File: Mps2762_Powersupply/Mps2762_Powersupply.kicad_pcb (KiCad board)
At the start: 4 copper layers, 56.7 x 37.7 mm, 52 parts, among them J1 124018312112A, J2 Conn_01x08_Pin, J3 Conn_01x02_Pin, J4 Conn_01x02_Pin, SW1 SW_DIP_x03, U1 MP2762AGV-0000-P, U2 CH224K, U3 AP62600SJ-7

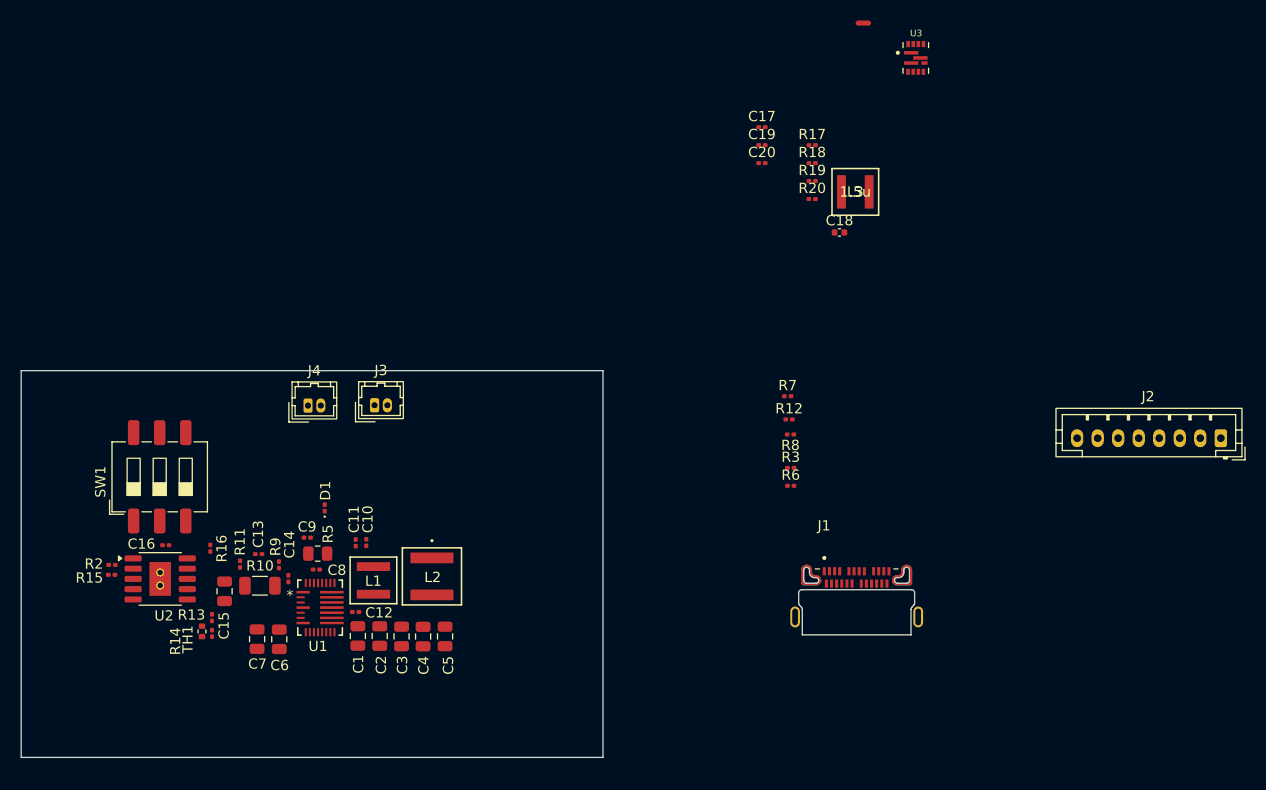
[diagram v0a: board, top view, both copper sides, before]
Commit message: layout updated
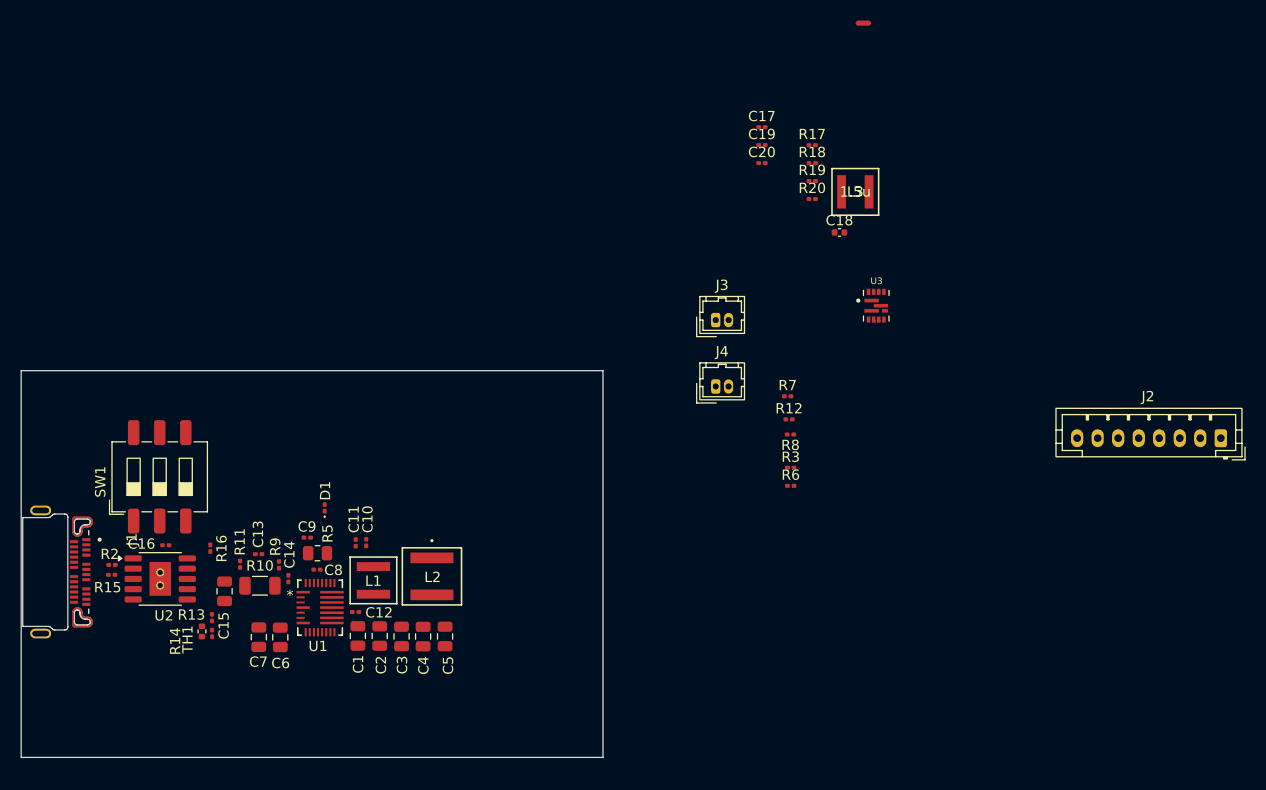
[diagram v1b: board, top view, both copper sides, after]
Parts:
- moved J1 79.6 mm to (108.7, 107.0), turned to -90 degrees
- moved J4 39.8 mm to (174.5, 88.9)
- moved J3 34.3 mm to (174.5, 82.5)
- moved U3 24.5 mm to (190.1, 81.0)
- moved C7 0.25 mm to (129.9, 113.3)
- moved C6 0.21 mm to (132.0, 113.4)
- moved C8 0.06 mm to (135.6, 106.8)

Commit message: added gnd vias
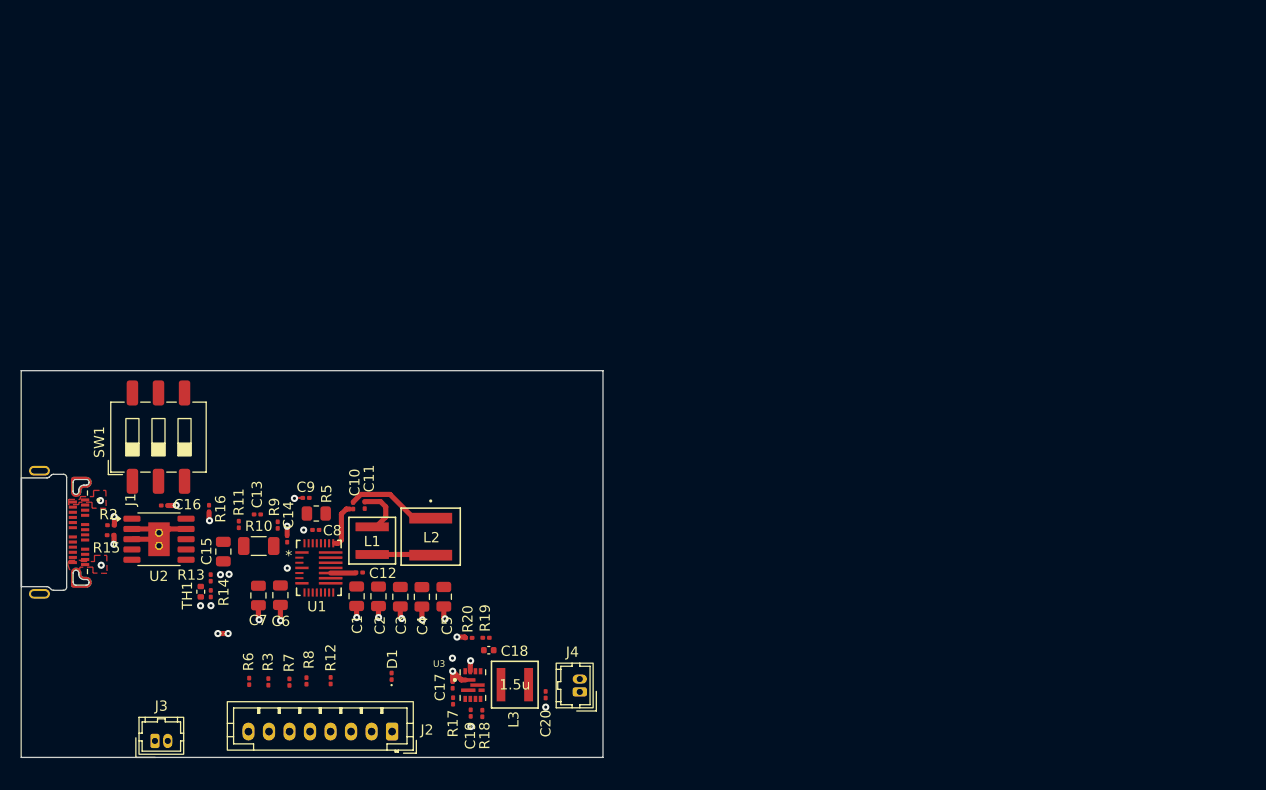
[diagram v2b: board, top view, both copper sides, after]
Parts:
- moved NT0 86.2 mm to (126.4, 113.0), turned to 180 degrees
- moved J2 85.7 mm to (142.9, 122.5)
- moved J3 68.3 mm to (119.8, 123.5)
- moved R17 64.5 mm to (148.9, 119.6), turned to -90 degrees
- moved R18 62.5 mm to (151.7, 120.8), turned to 90 degrees
- moved C19 62.2 mm to (150.6, 120.8), turned to -90 degrees
- moved C17 62.2 mm to (148.8, 118.0), turned to -90 degrees
- moved L3 58.4 mm to (154.9, 118.0)
- moved R6 56.1 mm to (129.0, 117.7), turned to 90 degrees
- moved R7 56.0 mm to (132.9, 117.7), turned to -90 degrees
- moved C20 55.9 mm to (157.9, 119.0), turned to 90 degrees
- moved R3 55.0 mm to (130.9, 117.7), turned to 90 degrees
- moved R19 54.7 mm to (152.1, 113.4)
- moved R20 54.3 mm to (150.4, 113.4)
- moved U3 54.0 mm to (150.8, 118.0)
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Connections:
- J2 pad 1: /PROCHOT -> /ACOK
- J2 pad 2: /INT -> /IAM
- J2 pad 3: /MCU_ACOK -> /IBM
- J2 pad 5: /IBM -> /SCL
- J2 pad 6: /IAM -> /SDA
- J2 pad 7: /SDA -> /INT
- J2 pad 8: /SCL -> /PROCHOT
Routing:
- net PGND: track 0.00 -> 27.4 mm, vias 0 -> 25
- net /SW1: track 0.00 -> 8.82 mm
- net /SW3: track 0.00 -> 8.22 mm
- net /SW2: track 0.00 -> 4.97 mm
- net /BST1: track 0.00 -> 4.46 mm
- net AGND: track 0.00 -> 0.03 mm, vias 0 -> 4
- added copper zone on In1.Cu, net AGND
- added copper zone on F.Cu, net PGND
- added copper zone on In2.Cu, net PGND

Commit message: almost routed
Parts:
- removed NT0: NetTie_2, NetTie:NetTie-2_SMD_Pad0.5mm
- C10: moved to B.Cu
- moved J3 46.3 mm to (161.6, 103.6), turned to 90 degrees
- moved R6 38.6 mm to (159.7, 94.2), turned to -90 degrees
- moved R3 36.2 mm to (158.4, 94.2), turned to -90 degrees
- moved J2 36.1 mm to (160.0, 90.7)
- moved R12 28.6 mm to (153.9, 94.5)
- moved R7 27.6 mm to (147.5, 94.3), turned to 90 degrees
- moved R8 26.0 mm to (145.9, 94.3), turned to 90 degrees
- moved D1 18.8 mm to (130.4, 103.2)
- moved L2 16.2 mm to (136.5, 90.9), turned to 0 degrees
- moved TH1 13.9 mm to (137.2, 114.1)
- moved C7 13.8 mm to (143.5, 106.7)
- moved R2 13.0 mm to (122.5, 91.5), turned to -90 degrees
- moved R15 12.8 mm to (119.9, 91.5), turned to -90 degrees
- moved R16 12.3 mm to (117.1, 91.5), turned to -90 degrees
- moved R14 12.1 mm to (136.0, 114.6)
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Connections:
- J2 pad 1: /ACOK -> /PROCHOT
- J2 pad 2: /IAM -> /INT
- J2 pad 3: /IBM -> /MCU_ACOK
- J2 pad 5: /SCL -> /IBM
- J2 pad 6: /SDA -> /IAM
- J2 pad 7: /INT -> /SDA
- J2 pad 8: /PROCHOT -> /SCL
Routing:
- net +3.3V: track 0.00 -> 47.1 mm, vias 0 -> 6
- net /PROCHOT: track 0.00 -> 29.8 mm
- net /INT: track 0.00 -> 29.0 mm
- net /PSYS: track 0.00 -> 23.6 mm, vias 0 -> 2
- net /SDA: track 0.00 -> 22.7 mm
- net /IBM: track 0.00 -> 21.1 mm, vias 0 -> 1
- net /IAM: track 0.00 -> 20.8 mm, vias 0 -> 1
- net /CC2: track 0.00 -> 20.3 mm
- net /SCL: track 0.00 -> 19.4 mm
- net /CC1: track 0.00 -> 19.2 mm
- net +5V: track 0.00 -> 16.3 mm
- net /SYS: track 0.00 -> 15.4 mm, vias 0 -> 9
- net Net-(U1-NTC/BATDET): track 0.00 -> 12.1 mm
- net Net-(U1-IAP): track 0.00 -> 11.2 mm
- net /VCC: track 0.00 -> 10.9 mm
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- added copper zone on B.Cu, net /BATT
- added copper zone on F.Cu, net /SW1
- added copper zone on F.Cu, net /SW2
- added copper zone on F.Cu, net /SW3
- added copper zone on B.Cu, net /SYS
- added copper zone on F.Cu, net /SYS
- added copper zone on B.Cu, net /VBUS
- added copper zone on F.Cu, net /VBUS
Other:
- board size 56.7 x 37.7 mm -> 57 x 39.1 mm
